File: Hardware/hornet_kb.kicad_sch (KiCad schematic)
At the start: 32 parts, among them J1 Conn_ST_STDC14, J10 USB_C_Receptacle_USB2.0, SW98 SW_Push, U1 nRF52840, Y1 32.768kHz, Y2 32MHz

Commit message: assign footprints (rough draft)
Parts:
- L3, L4: footprint (none) -> Inductor_SMD:L_0402_1005Metric
- SW98: footprint (none) -> Button_Switch_SMD:SW_Push_1P1T-MP_NO_Horizontal_Alps_SKRTLAE010
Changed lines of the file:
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@@
 			)
 		)
-		(property "Footprint" ""
+		(property "Footprint" "Button_Switch_SMD:SW_Push_1P1T-MP_NO_Horizontal_Alps_SKRTLAE010"
 			(at 52.07 180.34 0)
 			(effects
@@
 			)
 		)
-		(property "Footprint" ""
+		(property "Footprint" "Inductor_SMD:L_0402_1005Metric"
 			(at 135.89 71.12 0)
 			(effects
@@
 			)
 		)
-		(property "Footprint" ""
+		(property "Footprint" "Inductor_SMD:L_0402_1005Metric"
 			(at 127 62.23 0)
 			(effects

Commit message: delete stale comments and fix erc
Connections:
- net GND1 is gone; now on net GND: C3.1, C4.1
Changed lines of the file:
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@@
 	)
 	(junction
-		(at 279.4 123.19)
-		(diameter 0)
-		(color 0 0 0 0)
-	)
-	(junction
 		(at 255.27 83.82)
 		(diameter 0)
@@
 	)
 	(symbol
+		(lib_id "power:GND")
+		(at 64.77 147.32 0)
+		(mirror y)
+		(unit 1)
+		(exclude_from_sim no)
+		(in_bom yes)
+		(on_board yes)
+		(dnp no)
+		(property "Reference" "#PWR03"
+			(at 64.77 153.67 0)
+			(effects
+				(font
+					(size 1.27 1.27)
+				)
+				(hide yes)
+			)
+		)
+		(property "Value" "GND"
+			(at 65.024 152.146 0)
+			(effects
+				(font
+					(size 1.27 1.27)
+				)
+			)
+		)
+		(property "Footprint" ""
+			(at 64.77 147.32 0)
+			(effects
+				(font
+					(size 1.27 1.27)
+				)
+				(hide yes)
+			)
+		)
+		(property "Datasheet" ""
+			(at 64.77 147.32 0)
+			(effects
+				(font
+					(size 1.27 1.27)
+				)
+				(hide yes)
+			)
+		)
+		(property "Description" "Power symbol creates a global label with name \"GND\" , ground"
+			(at 64.77 147.32 0)
+			(effects
+				(font
+					(size 1.27 1.27)
+				)
+				(hide yes)
+			)
+		)
+		(pin "1"
+		)
+		(instances
+			(project "hornet_kb"
+				(path "/c35084ab-104c-4a4c-9388-a839989b8e3d"
+					(reference "#PWR03")
+					(unit 1)
+				)
+			)
+		)
+	)
+	(symbol
 		(lib_id "Connector:Conn_ST_STDC14")
 		(at 273.05 43.18 0)
@@
 	)
 	(symbol
-		(lib_id "power:PWR_FLAG")
-		(at 279.4 123.19 180)
-		(unit 1)
-		(exclude_from_sim no)
-		(in_bom yes)
-		(on_board yes)
-		(dnp no)
-		(fields_autoplaced yes)
-		(property "Reference" "#FLG03"
-			(at 279.4 125.095 0)
-			(effects
-				(font
-					(size 1.27 1.27)
-				)
-				(hide yes)
-			)
-		)
-		(property "Value" "PWR_FLAG"
-			(at 279.4 128.27 0)
-			(effects
-				(font
-					(size 1.27 1.27)
-				)
-			)
-		)
-		(property "Footprint" ""
-			(at 279.4 123.19 0)
-			(effects
-				(font
-					(size 1.27 1.27)
-				)
-				(hide yes)
-			)
-		)
-		(property "Datasheet" "~"
-			(at 279.4 123.19 0)
-			(effects
-				(font
-					(size 1.27 1.27)
-				)
-				(hide yes)
-			)
-		)
-		(property "Description" "Special symbol for telling ERC where power comes from"
-			(at 279.4 123.19 0)
-			(effects
-				(font
-					(size 1.27 1.27)
-				)
-				(hide yes)
-			)
-		)
-		(pin "1"
-		)
-		(instances
-			(project "hornet_kb"
-				(path "/c35084ab-104c-4a4c-9388-a839989b8e3d"
-					(reference "#FLG03")
-					(unit 1)
-				)
-			)
-		)
-	)
-	(symbol
 		(lib_id "Device:Antenna")
 		(at 39.37 91.44 0)
@@
 					(unit 1)
 				)
-			)
-		)
-	)
-	(symbol
-		(lib_id "power:GND1")
-		(at 64.77 147.32 0)
-		(mirror y)
-		(unit 1)
-		(exclude_from_sim no)
-		(in_bom yes)
-		(on_board yes)
-		(dnp no)
-		(fields_autoplaced yes)
-		(property "Reference" "#PWR03"
-			(at 64.77 153.67 0)
-			(effects
-				(font
-					(size 1.27 1.27)
-				)
-				(hide yes)
-			)
-		)
-		(property "Value" "GND1"
-			(at 64.77 152.4 0)
-			(effects
-				(font
-					(size 1.27 1.27)
-				)
-			)
-		)
-		(property "Footprint" ""
-			(at 64.77 147.32 0)
-			(effects
-				(font
-					(size 1.27 1.27)
-				)
-				(hide yes)
-			)
-		)
-		(property "Datasheet" ""
-			(at 64.77 147.32 0)
-			(effects
-				(font
-					(size 1.27 1.27)
-				)
-				(hide yes)
-			)
-		)
-		(property "Description" "Power symbol creates a global label with name \"GND1\" , ground"
-			(at 64.77 147.32 0)
-			(effects
-				(font
-					(size 1.27 1.27)
-				)
-				(hide yes)
-			)
-		)
-		(pin "1"
-		)
-		(instances
-			(project "hornet_kb"
-				(path "/c35084ab-104c-4a4c-9388-a839989b8e3d"
-					(reference "#PWR03")
-					(unit 1)
-				)

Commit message: Route dual sided hotswap/diodes assmebly
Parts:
- AE1: now left out of the parts list
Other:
- note added: "stable 3V3 output by nrf's built-in LDO"
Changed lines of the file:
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@@
 		)
 	)
-	(text "Raw battery \noutput"
+	(text "Raw battery\noutput"
 		(exclude_from_sim no)
-		(at 121.666 26.416 0)
+		(at 116.332 26.162 0)
 		(effects
 			(font
 				(size 1.27 1.27)
 			)
-			(justify left)
+			(justify right)
 		)
 	)
@@
 		)
 	)
+	(text "stable 3V3 output by \nnrf's built-in LDO"
+		(exclude_from_sim no)
+		(at 149.352 37.338 0)
+		(effects
+			(font
+				(size 1.27 1.27)
+			)
+			(justify left)
+		)
+	)
 	(text "reset either by physical button or STLINK"
 		(exclude_from_sim no)
@@
 		(unit 1)
 		(exclude_from_sim no)
-		(in_bom yes)
-		(on_board yes)
+		(in_bom no)
+		(on_board no)
 		(dnp no)
 		(property "Reference" "AE1"

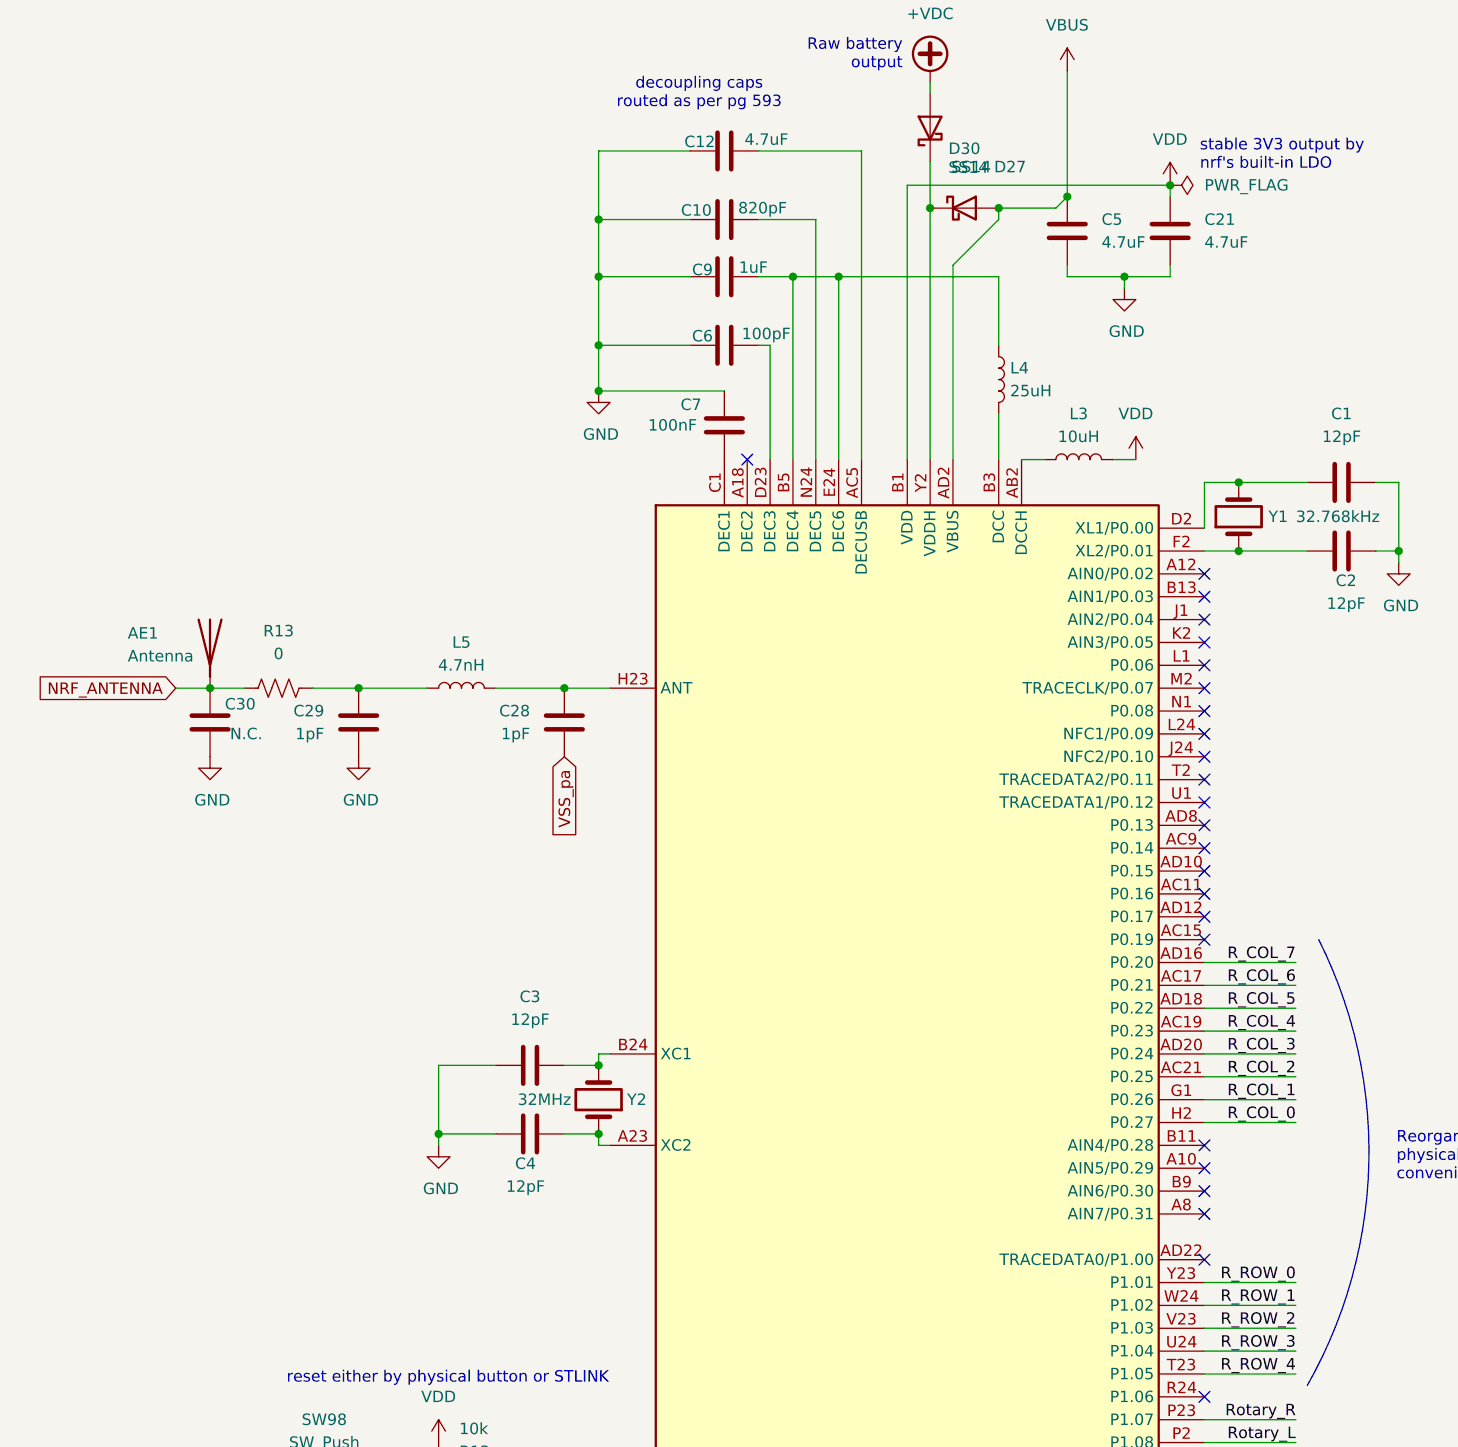
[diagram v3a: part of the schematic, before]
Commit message: added extra decoupling caps to the mcu VDD pins
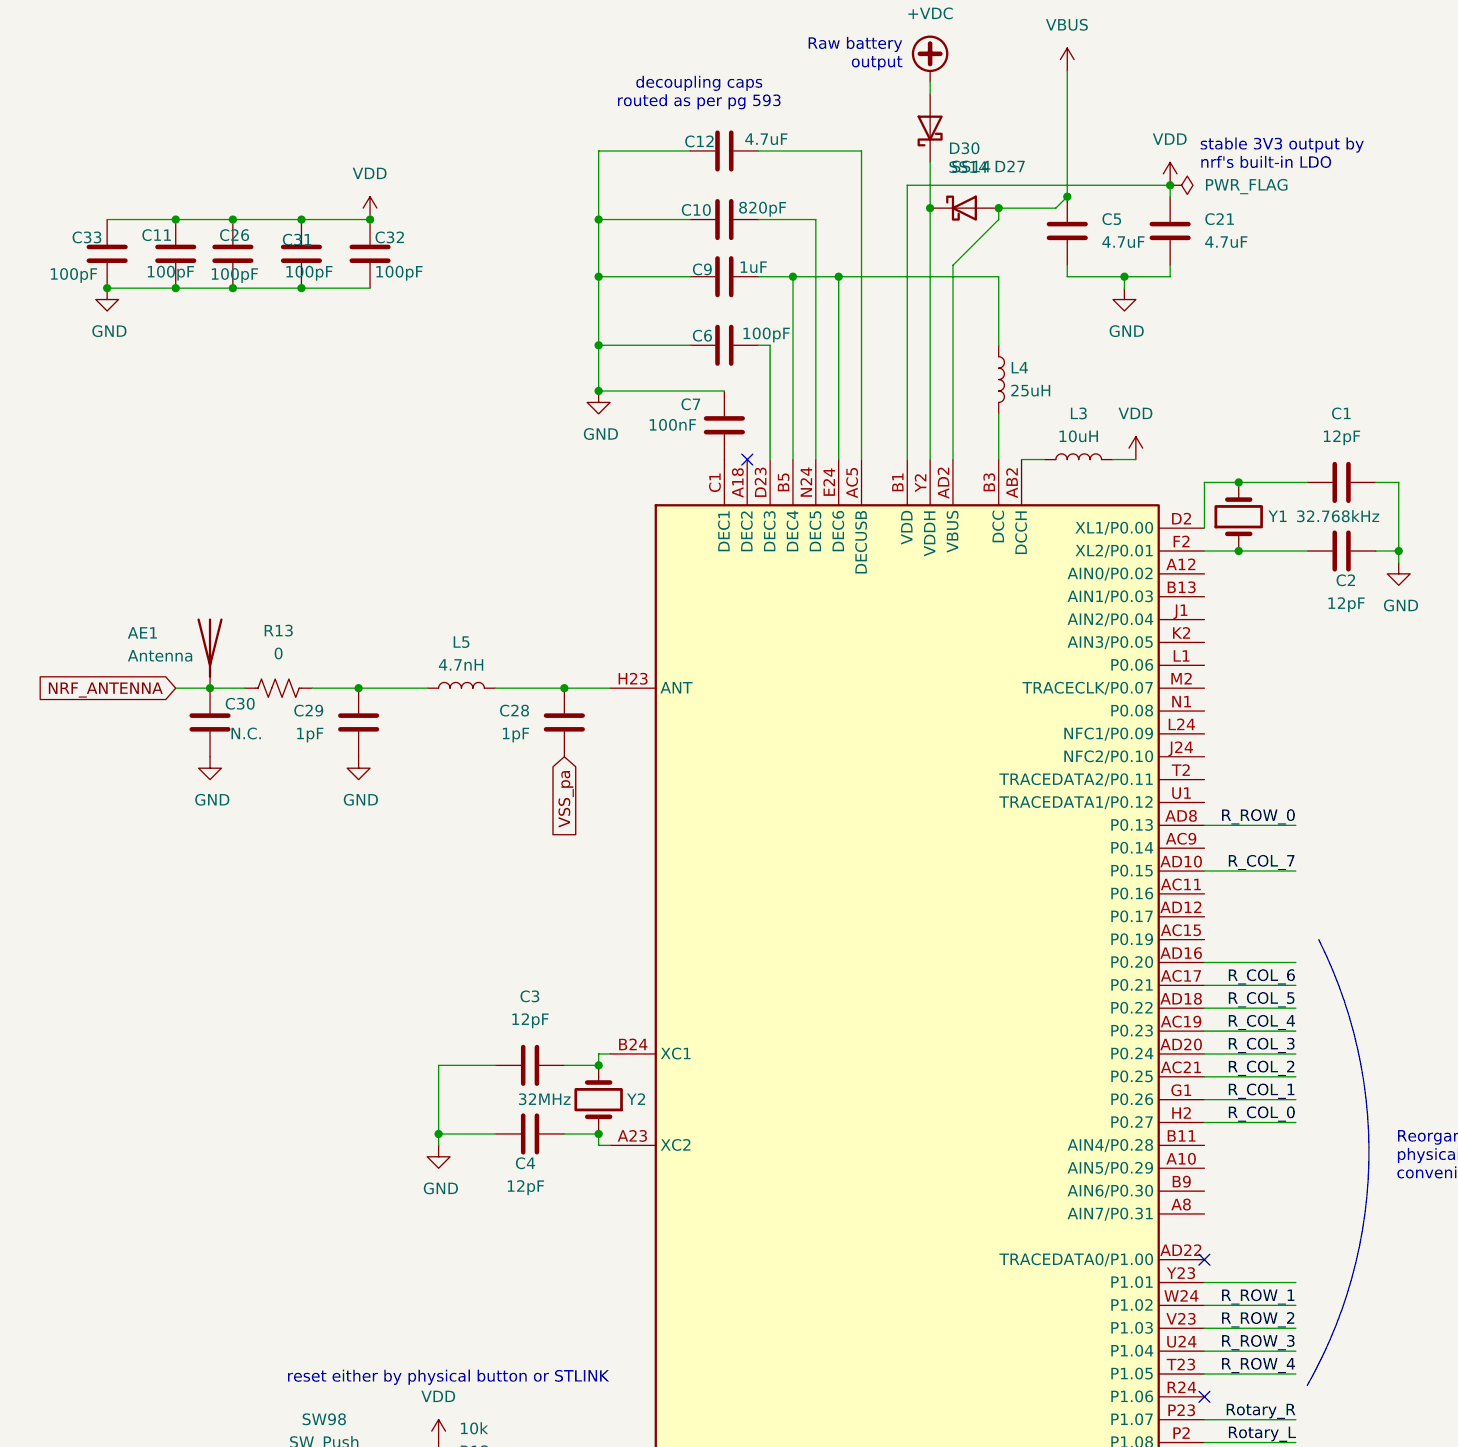
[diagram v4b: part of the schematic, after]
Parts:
- added C11, C26, C31, C32, C33: 100pF, Capacitor_SMD:C_0603_1608Metric, symbol Device:C
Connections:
- net GND: now also C11.2, C26.2, C31.2, C32.2, C33.2
- net R_COL_7: now also U1.AD10 (P0.15); no longer U1.AD16 (P0.20)
- net R_ROW_0: now also U1.AD8 (P0.13); no longer U1.Y23 (P1.01)
- net VDD: now also C11.1, C26.1, C31.1, C32.1, C33.1
- no-connect marks 33 -> 12

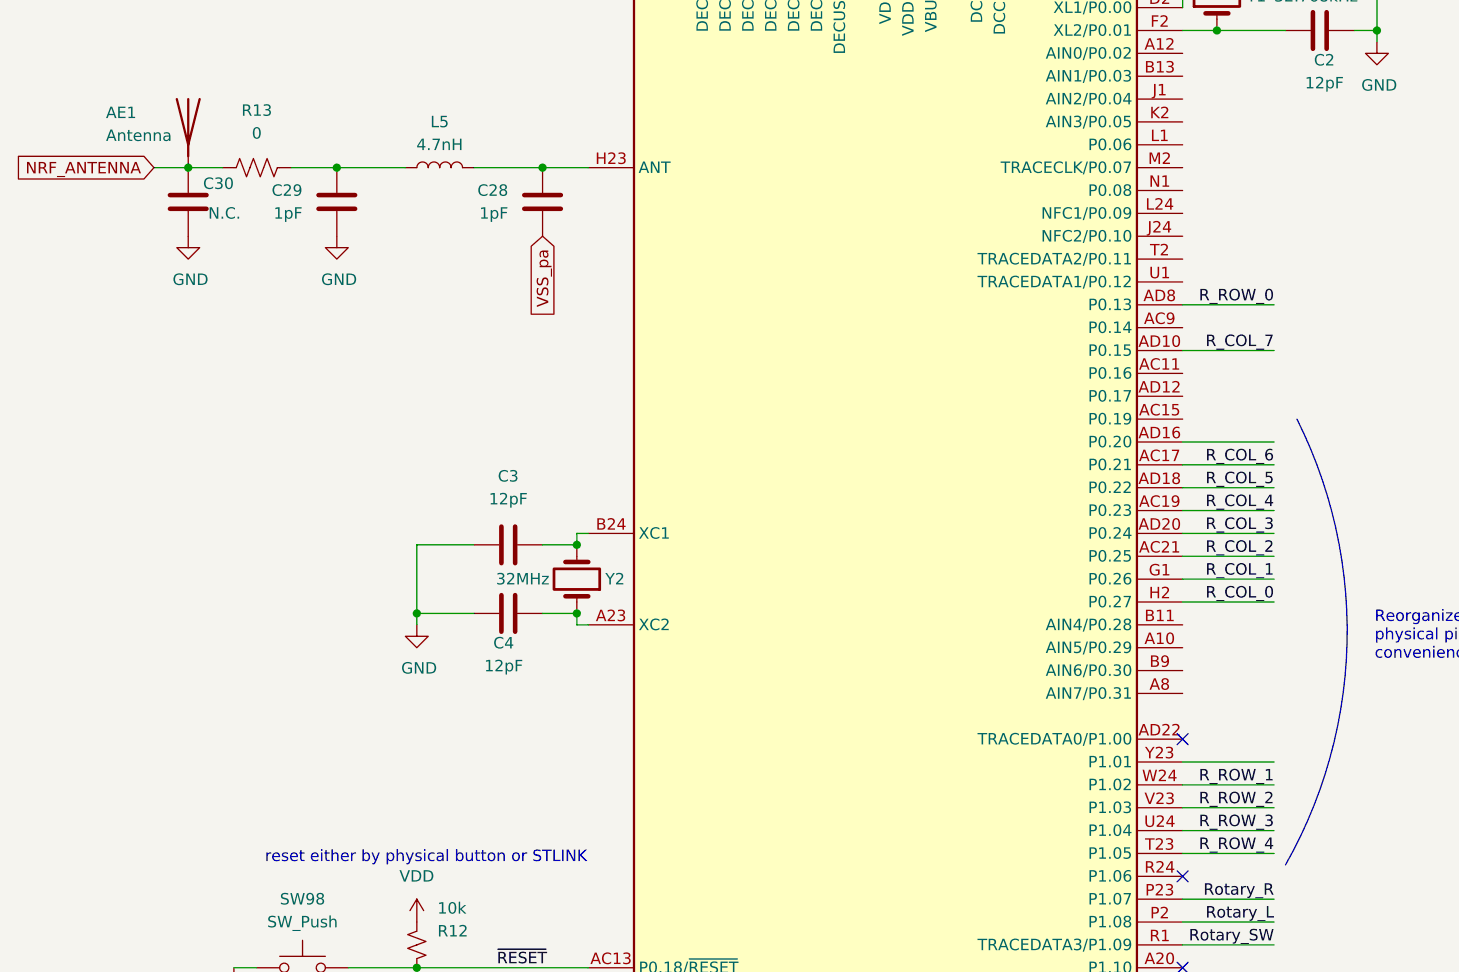
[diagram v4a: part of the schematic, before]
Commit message: move MCU to prioritize BLE routing
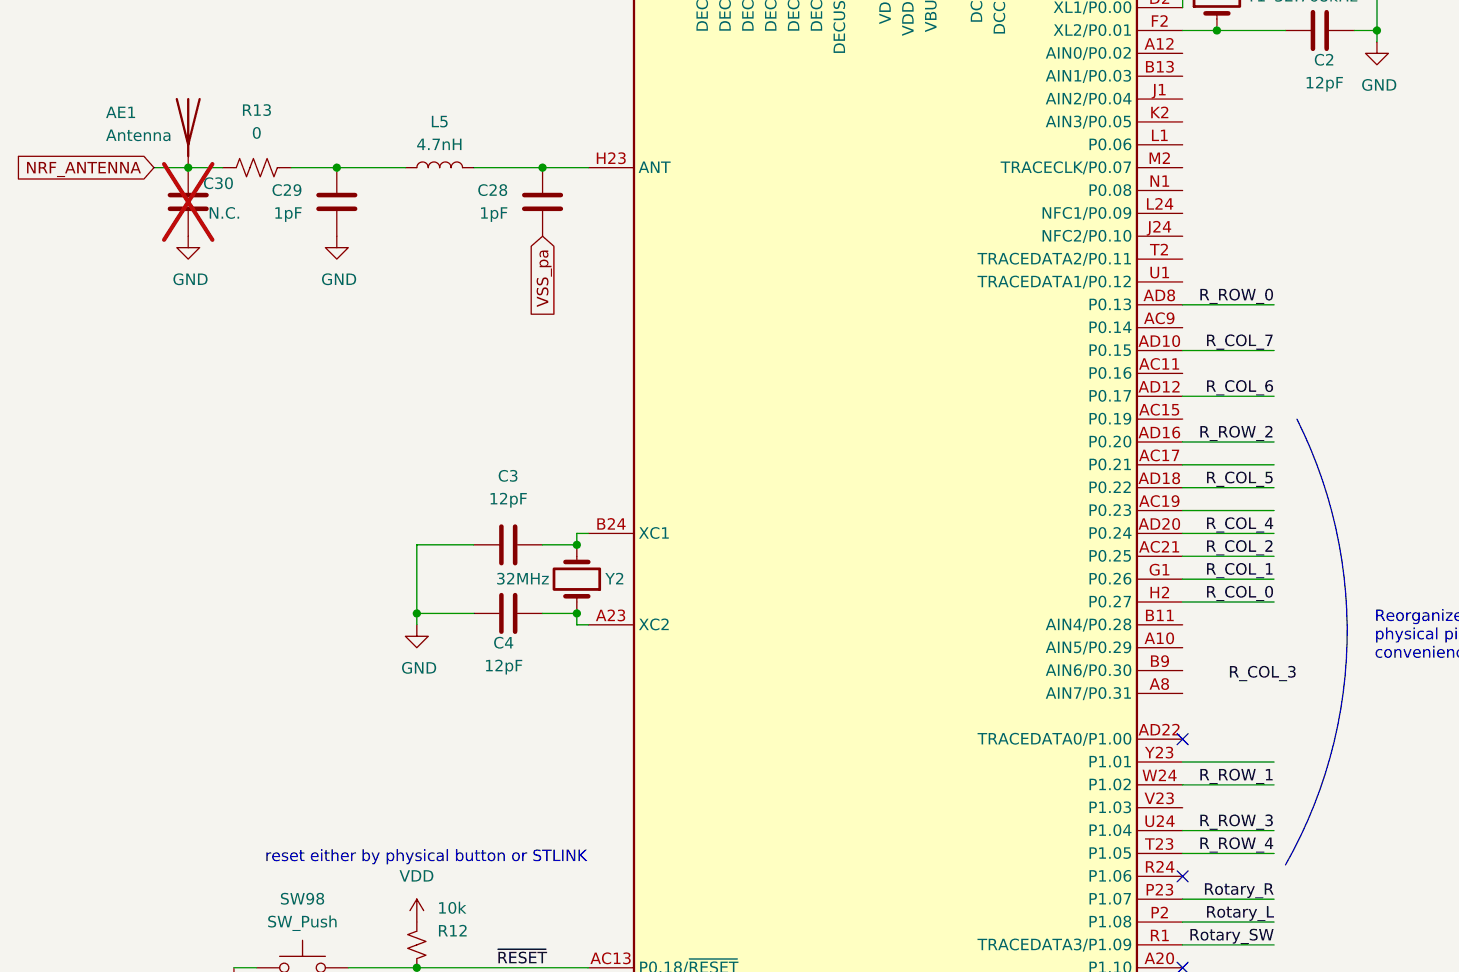
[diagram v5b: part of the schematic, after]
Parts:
- C30: now not fitted; now left out of the parts list
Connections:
- net R_COL_3: no longer U1.AD20 (P0.24)
- net R_COL_4: now also U1.AD20 (P0.24); no longer U1.AC19 (P0.23)
- net R_COL_6: now also U1.AD12 (P0.17); no longer U1.AC17 (P0.21)
- net R_ROW_2: now also U1.AD16 (P0.20); no longer U1.V23 (P1.03)
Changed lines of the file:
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@@
 	(wire
 		(pts
-			(xy 160.02 127) (xy 149.86 127)
-		)
-		(stroke
-			(width 0)
-			(type default)
-		)
-	)
-	(wire
-		(pts
 			(xy 160.02 177.8) (xy 149.86 177.8)
 		)
@@
 	(wire
 		(pts
+			(xy 160.02 127) (xy 149.86 127)
+		)
+		(stroke
+			(width 0)
+			(type default)
+		)
+	)
+	(wire
+		(pts
 			(xy 134.62 50.8) (xy 140.97 50.8)
 		)
@@
 	(wire
 		(pts
+			(xy 160.02 121.92) (xy 149.86 121.92)
+		)
+		(stroke
+			(width 0)
+			(type default)
+		)
+	)
+	(wire
+		(pts
 			(xy 207.01 179.07) (xy 217.17 179.07)
 		)
@@
 		)
 	)
-	(wire
-		(pts
-			(xy 160.02 167.64) (xy 149.86 167.64)
-		)
-		(stroke
-			(width 0)
-			(type default)
-		)
-	)
 	(image
 		(at 237.49 175.26)
@@
 		)
 	)
+	(label "R_COL_6"
+		(at 160.02 121.92 180)
+		(effects
+			(font
+				(size 1.27 1.27)
+			)
+			(justify right bottom)
+		)
+	)
 	(label "COMPRT_RX"
 		(at 162.56 195.58 180)
@@
 		)
 	)
+	(label "R_COL_3"
+		(at 162.56 153.67 180)
+		(effects
+			(font
+				(size 1.27 1.27)
+			)
+			(justify right bottom)
+		)
+	)
 	(label "R_COL_5"
 		(at 160.02 132.08 180)
@@
 		)
 	)
-	(label "R_COL_6"
-		(at 160.02 129.54 180)
+	(label "R_COL_4"
+		(at 160.02 137.16 180)
 		(effects
 			(font
@@
 		)
 	)
-	(label "R_ROW_2"
-		(at 160.02 167.64 180)
-		(effects
-			(font
-				(size 1.27 1.27)
-			)
-			(justify right bottom)
-		)
-	)
 	(label "R_ROW_0"
 		(at 207.01 167.64 0)
@@
 		)
 	)
-	(label "R_COL_4"
-		(at 160.02 134.62 180)
+	(label "R_ROW_2"
+		(at 160.02 127 180)
 		(effects
 			(font
@@
 		)
 	)
-	(label "R_COL_3"
-		(at 160.02 137.16 180)
-		(effects
-			(font
-				(size 1.27 1.27)
-			)
-			(justify right bottom)
-		)
-	)
 	(label "R_ROW_3"
 		(at 160.02 170.18 180)
@@
 		(unit 1)
 		(exclude_from_sim no)
-		(in_bom yes)
-		(on_board yes)
-		(dnp no)
+		(in_bom no)
+		(on_board no)
+		(dnp yes)
 		(property "Reference" "C30"
 			(at 44.45 98.298 0)
